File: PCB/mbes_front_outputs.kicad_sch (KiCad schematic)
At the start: 57 parts, among them Q1 BC817, Q10 BC817, Q11 TPCA8120,L1Q, Q14 BC817, Q15 BC817, Q19 BC817, Q2 BC817, Q20 BC817, Q21 BC817, Q4 TPCA8120,L1Q, Q5 TPCA8120,L1Q, Q6 TPCA8120,L1Q, Q7 TPCA8120,L1Q, Q8 TPCA8120,L1Q

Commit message: First uncompleted release
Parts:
- renumbered F2 to F1, Q14 to Q10, Q15 to Q11, Q6 to Q12, Q19 to Q13, Q20 to Q14, Q21 to Q15, Q7 to Q16, Q10 to Q17, Q8 to Q18, Q11 to Q5, Q4 to Q6, Q5 to Q7, Q1 to Q8, Q2 to Q9, RA25 to RA10, RA26 to RA11, RA27 to RA12, RA28 to RA13, RA9 to RA14, RA10 to RA15, RA11 to RA16, RA12 to RA17, RA13 to RA18, RA14 to RA19, RA34 to RA20, RA42 to RA21, RA35 to RA22, RA36 to RA23, RA37 to RA24, RA38 to RA25, RA7 to RA26, RA39 to RA27, RA40 to RA28, RA23 to RA29, RA2 to RA3, RA16 to RA30, RA17 to RA31, RA18 to RA32, RA19 to RA33, RA20 to RA34, RA21 to RA35, RA22 to RA36, RA1 to RA4, RA3 to RA5, RA4 to RA6, RA5 to RA7, RA6 to RA8, RA24 to RA9

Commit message: updates
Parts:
- F1: footprint MSMF050-2:FUSE_F050-2 -> MF-MSMF050-2:FUSE_F050-2
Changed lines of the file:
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@@
 			)
 		)
-		(property "Footprint" "MSMF050-2:FUSE_F050-2"
+		(property "Footprint" "MF-MSMF050-2:FUSE_F050-2"
 			(at 174.752 157.226 0)
 			(effects

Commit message: Enhancement: the last BC337 has been replaced by a BC817
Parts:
- RA18, RA19: value 120 -> 33K
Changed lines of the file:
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@@
 			)
 		)
-		(property "Value" "120"
+		(property "Value" "33K"
 			(at 64.1858 67.7926 90)
 			(effects
@@
 			)
 		)
-		(property "Value" "120"
+		(property "Value" "33K"
 			(at 67.4878 67.7926 90)
 			(effects

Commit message: Small fixes
- Floating BC817's base fixed
- EngReady_LED connector orientation fixed
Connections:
- net +12V: now also engReadyLed1.2 (Pin_2); no longer engReadyLed1.1 (Pin_1)
- net at RA14.2: now also engReadyLed1.1 (Pin_1); no longer engReadyLed1.2 (Pin_2)
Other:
- moved on the sheet: engReadyLed1
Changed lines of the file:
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@@
 	(symbol
 		(lib_id "Connector_Generic:Conn_01x02")
-		(at 34.544 104.14 0)
-		(mirror y)
+		(at 34.544 106.68 180)
 		(unit 1)
 		(exclude_from_sim no)
@@
 		(dnp no)
 		(property "Reference" "engReadyLed1"
-			(at 34.671 101.219 0)
+			(at 34.671 109.601 0)
 			(effects
 				(font
@@
 		)
 		(property "Value" "Conn_01x02"
-			(at 34.544 100.584 0)
+			(at 34.544 110.236 0)
 			(effects
 				(font
@@
 		)
 		(property "Footprint" "Connector_PinHeader_2.54mm:PinHeader_1x02_P2.54mm_Vertical"
-			(at 34.544 104.14 0)
+			(at 34.544 106.68 0)
 			(effects
 				(font
@@
 		)
 		(property "Datasheet" "~"
-			(at 34.544 104.14 0)
+			(at 34.544 106.68 0)
 			(effects
 				(font
@@
 		)
 		(property "Description" ""
-			(at 34.544 104.14 0)
+			(at 34.544 106.68 0)
 			(effects
 				(font

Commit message: Connectors changing
In order to reuse the already used cables, all the input signal connectors have been changed from solder-wires-sockets to pin-header connectors.
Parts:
- DownLight_p1, Horn_p1, UpLight_p1, addLight_p1: footprint Connector_Wire:SolderWire-1.5sqmm_1x02_P6mm_D1.7mm_OD3mm -> Connector_Wire:SolderWire-1sqmm_1x02_P5.4mm_D1.4mm_OD2.7mm
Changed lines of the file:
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@@
 			)
 		)
-		(property "Footprint" "Connector_Wire:SolderWire-1.5sqmm_1x02_P6mm_D1.7mm_OD3mm"
+		(property "Footprint" "Connector_Wire:SolderWire-1sqmm_1x02_P5.4mm_D1.4mm_OD2.7mm"
 			(at 86.5632 176.1744 0)
 			(effects
@@
 			)
 		)
-		(property "Footprint" "Connector_Wire:SolderWire-1.5sqmm_1x02_P6mm_D1.7mm_OD3mm"
+		(property "Footprint" "Connector_Wire:SolderWire-1sqmm_1x02_P5.4mm_D1.4mm_OD2.7mm"
 			(at 202.184 161.036 0)
 			(effects
@@
 			)
 		)
-		(property "Footprint" "Connector_Wire:SolderWire-1.5sqmm_1x02_P6mm_D1.7mm_OD3mm"
+		(property "Footprint" "Connector_Wire:SolderWire-1sqmm_1x02_P5.4mm_D1.4mm_OD2.7mm"
 			(at 61.6204 176.1744 0)
 			(effects
@@
 			)
 		)
-		(property "Footprint" "Connector_Wire:SolderWire-1.5sqmm_1x02_P6mm_D1.7mm_OD3mm"
+		(property "Footprint" "Connector_Wire:SolderWire-1sqmm_1x02_P5.4mm_D1.4mm_OD2.7mm"
 			(at 30.5054 176.3522 0)
 			(effects

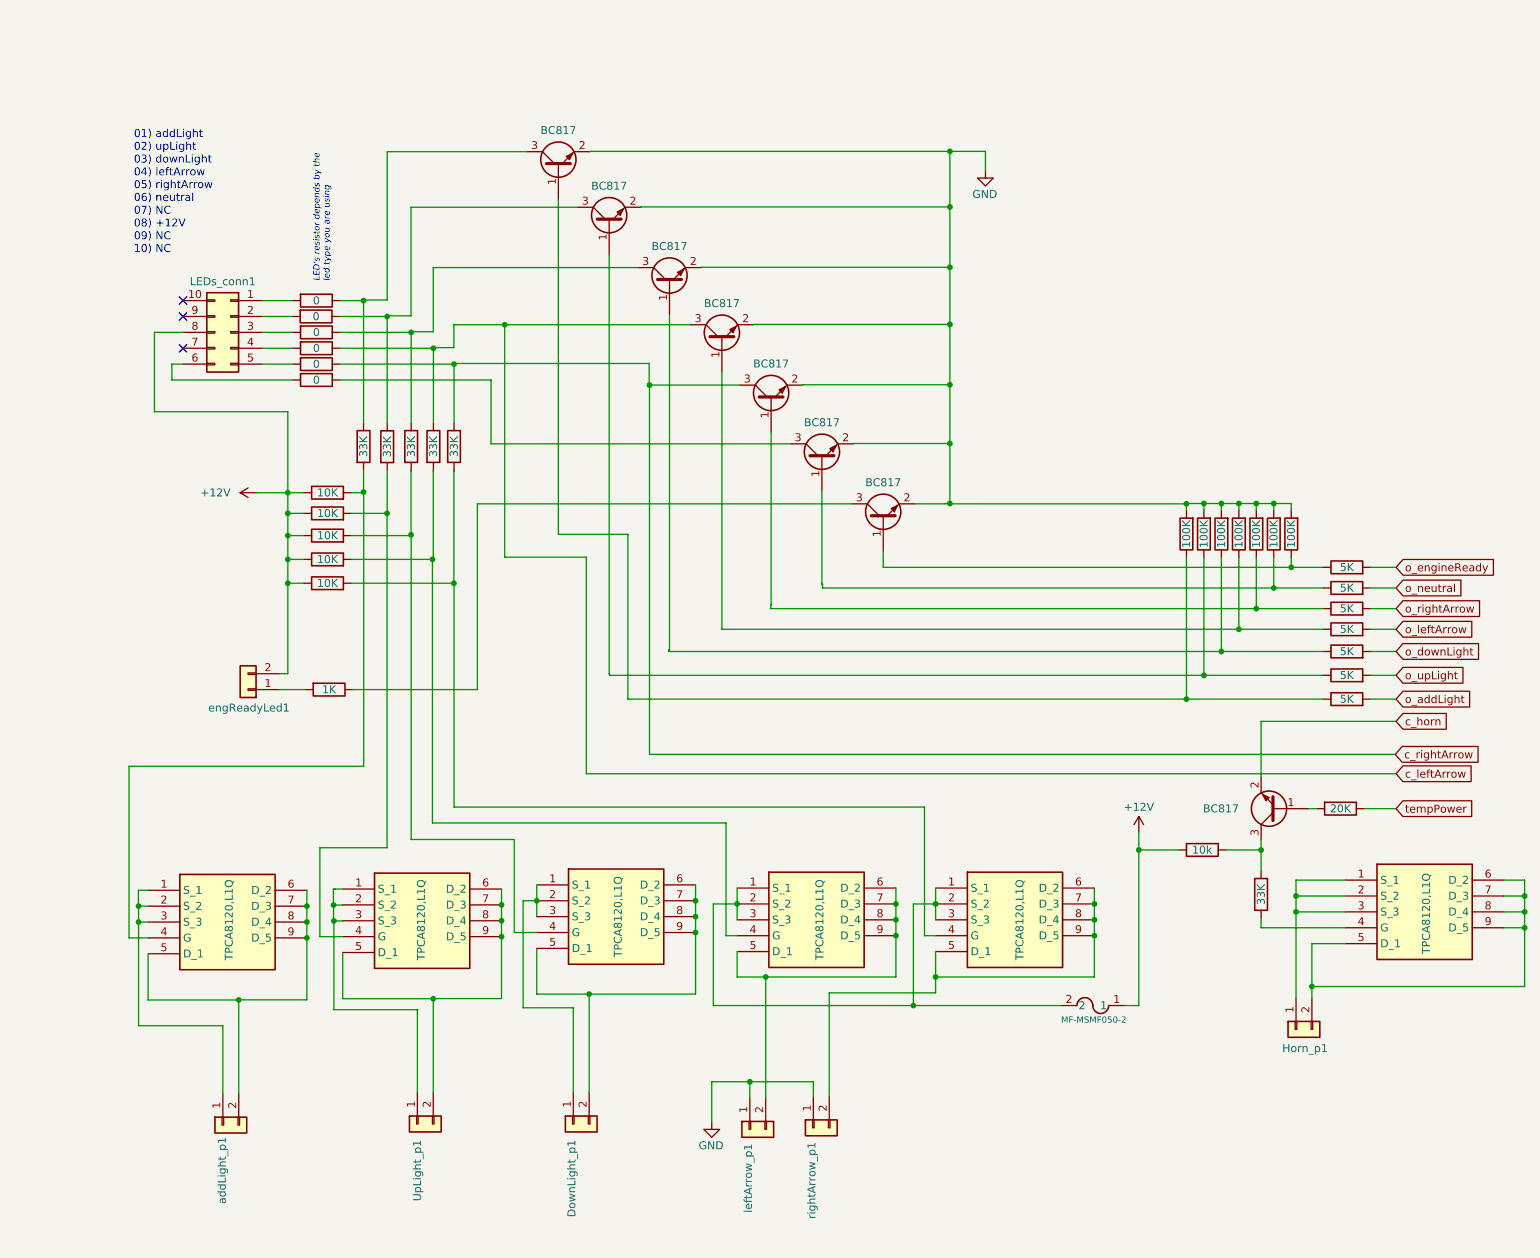
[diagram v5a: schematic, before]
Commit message: Many fixes and changes
- Electric schema and PCB changes:
	- To avoid unwanted service starting (lights, electric start engine....), the signals from the motorbike's front side to
	  the rear one, are no more connedted to the FET's gate directly. There is a second stage realized with PNPs transistors,
	  now. It is a more stable and safe solution.

- In the shcema:
	- All the c_<signal> symbols have been splitted in ci_<signal> and co_<signal>, and the symbols direction (input/output)
	  have been fixed
	- To get a more readable schema, the c*_<signal> symbols have a different color
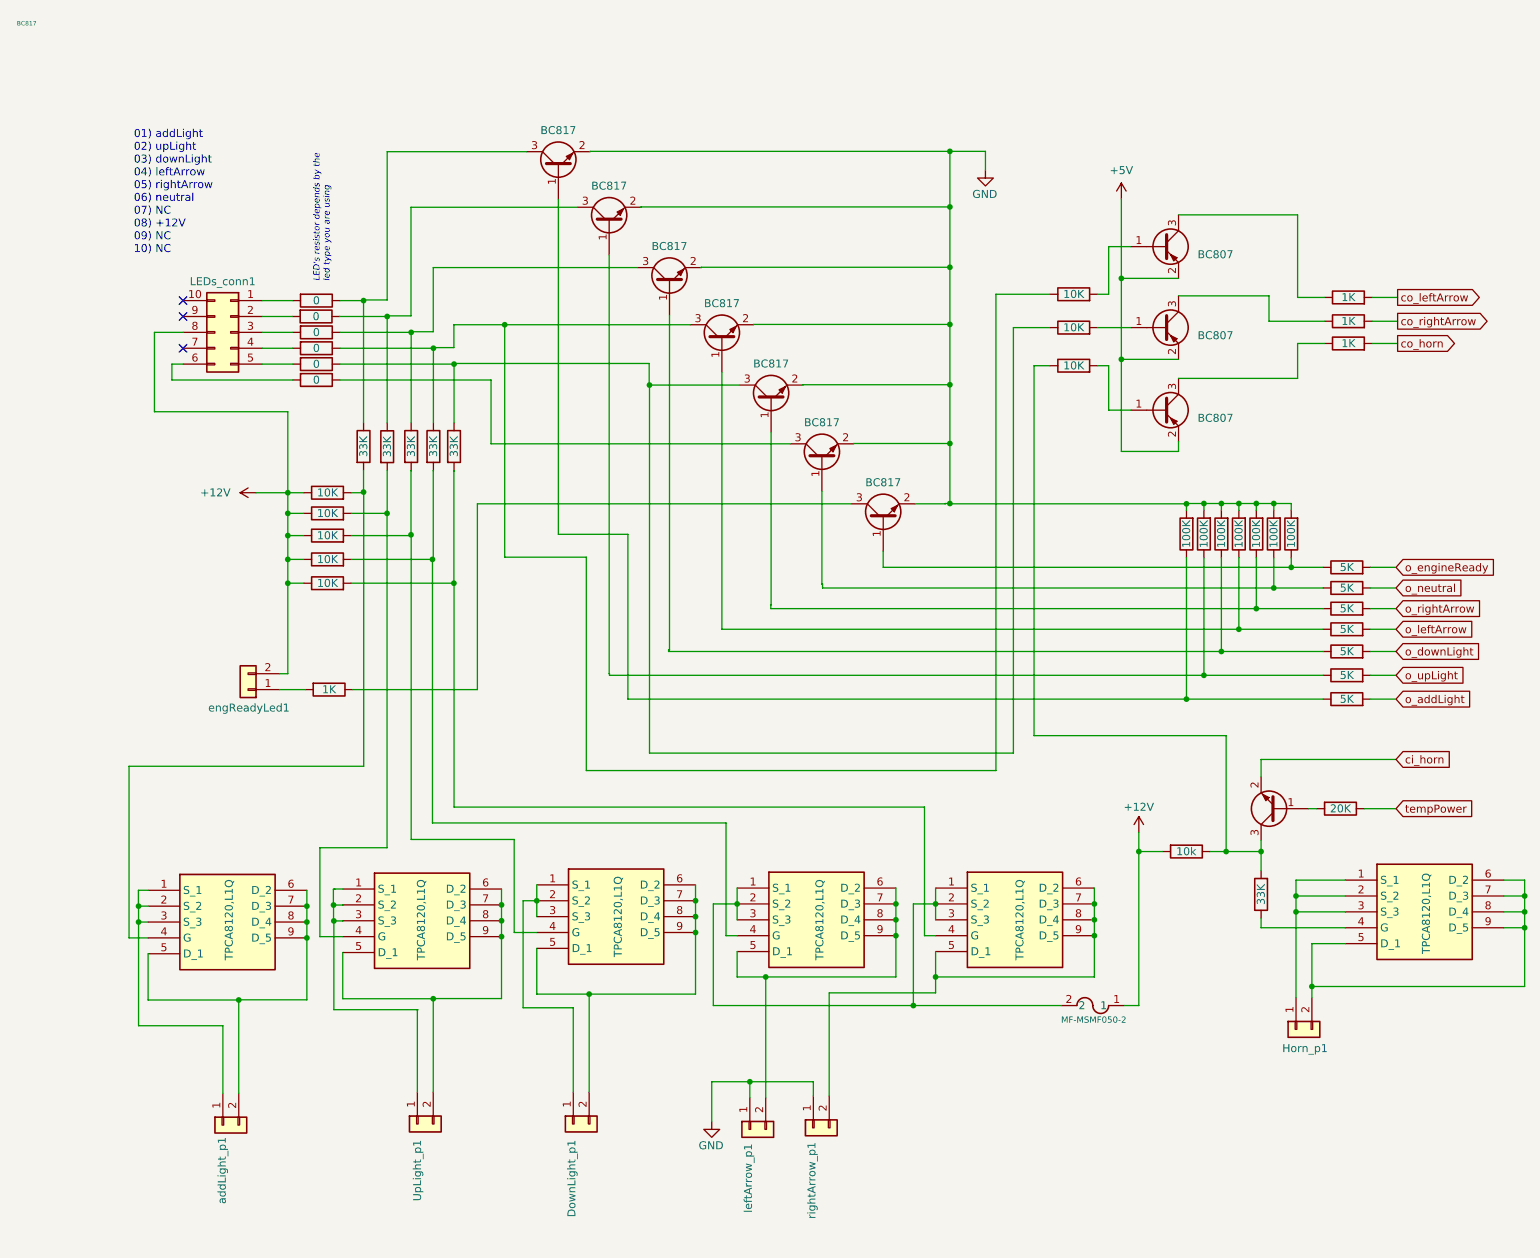
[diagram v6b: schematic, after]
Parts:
- added Q1, Q20, Q21: BC807, Package_TO_SOT_SMD:SOT-23, symbol Transistor_BJT:BC807
- added RA37, RA38, RA39: 10K, Resistor_SMD:R_1206_3216Metric, symbol Device:R
- added RA43, RA44, RA45: 1K, Resistor_SMD:R_1206_3216Metric, symbol Device:R
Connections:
- net at Q17.3 (C), RA21.1, RA26.2: now also RA39.1
- net c_horn renamed ci_horn
- net c_leftArrow: no longer names the net of Q11.3 (C), RA18.1, RA6.1
- net c_leftArrow: now also RA37.1
- net c_rightArrow: no longer names the net of Q13.3 (C), RA19.1, RA7.1
- net c_rightArrow: now also RA38.1
- new net: Q20.1 (B), RA38.2
- new net: Q21.3 (C), RA45.1
- new net: Q1.1 (B), RA37.2
- new net: Q21.1 (B), RA39.2
- new net: Q1.3 (C), RA43.1
- new net: Q20.3 (C), RA44.1
- new net +5V: Q1.2 (E), Q20.2 (E), Q21.2 (E)
- new net co_horn: RA45.2
- new net co_leftArrow: RA43.2
- new net co_rightArrow: RA44.2

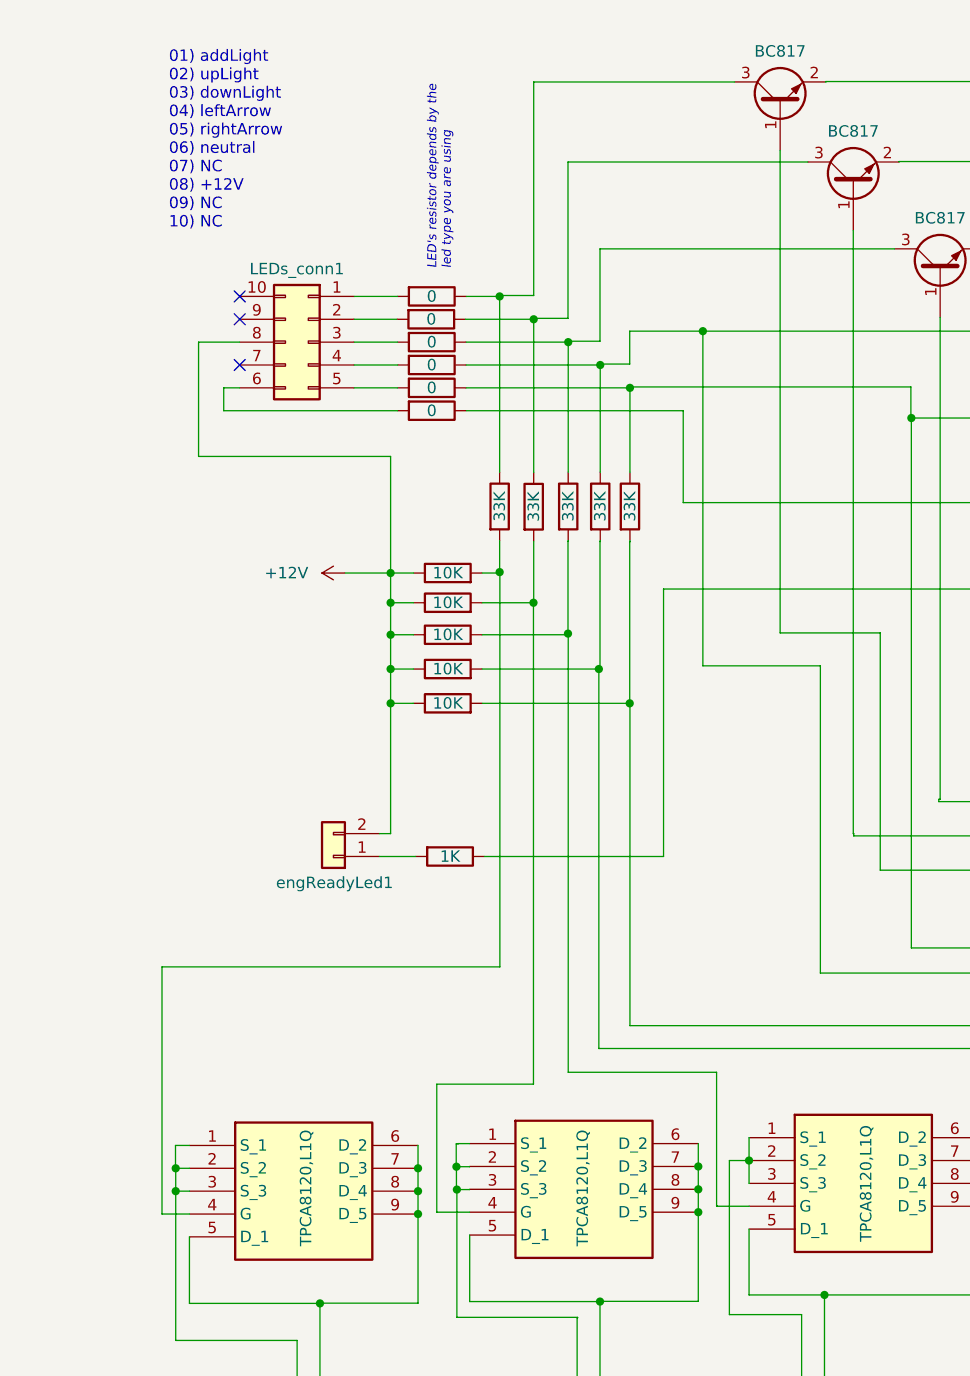
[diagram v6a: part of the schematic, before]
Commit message: FET's Gate to NPN's collector resistor removed
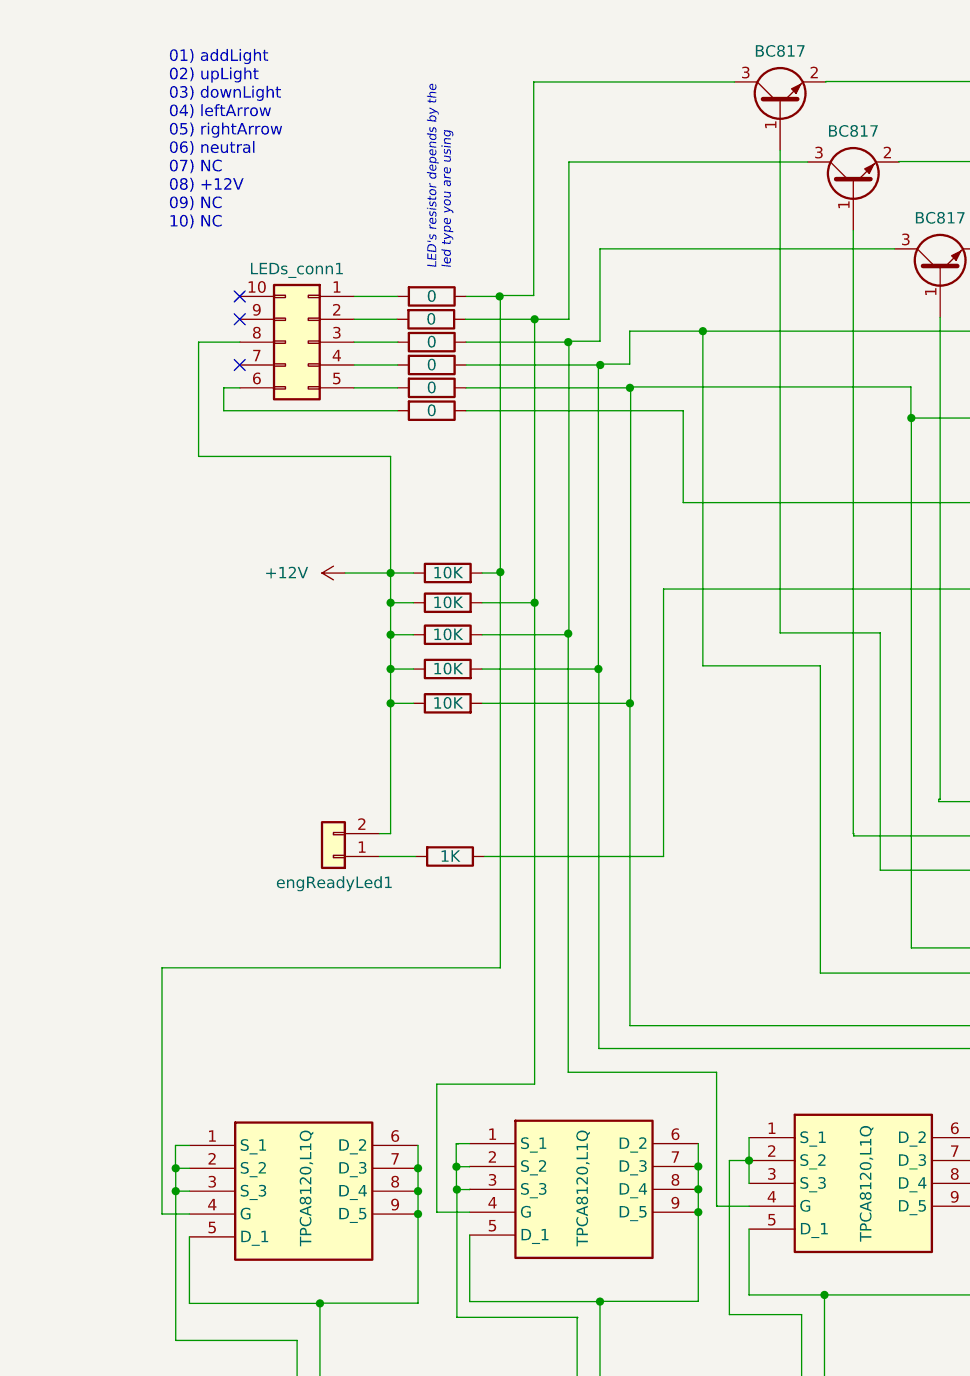
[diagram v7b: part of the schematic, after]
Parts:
- removed RA15, RA16, RA17, RA18, RA19: 33K, Resistor_SMD:R_1206_3216Metric, symbol Device:R
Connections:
- net at Q13.3 (C), RA38.1, RA7.1: now also Q16.4 (G), RA13.2
- net at Q8.3 (C), RA4.1: now also Q5.4 (G), RA9.2
- net at Q11.3 (C), RA37.1, RA6.1: now also Q12.4 (G), RA12.2
- net at Q7.4 (G), RA11.2: now also Q10.3 (C), RA5.1
- net at Q6.4 (G), RA10.2: now also Q9.3 (C), RA3.1
